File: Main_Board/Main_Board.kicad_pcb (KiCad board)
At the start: 2 copper layers, 3 parts, among them U1 TCR2EF33_LMCT

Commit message: Main board
The schematic is done, tho I have some concerns...
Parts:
- removed C1, C2: C, Capacitor_SMD:C_1206_3216Metric_Pad1.33x1.80mm_HandSolder
- added C3: 10uF, Capacitor_SMD:C_0805_2012Metric_Pad1.18x1.45mm_HandSolder, F.Cu at (173.5, 136.5)
- added C4: 0.1uF, Capacitor_SMD:C_0805_2012Metric_Pad1.18x1.45mm_HandSolder, F.Cu at (163.0, 136.5)
- added C5: 100uF, Capacitor_SMD:C_0805_2012Metric_Pad1.18x1.45mm_HandSolder, F.Cu at (168.5, 136.5)
- added J1: USB_C_Receptacle_USB2.0_16P, Connector_USB:USB_C_Receptacle_HRO_TYPE-C-31-M-17, F.Cu at (156.0, 147.0)
- added J2: Conn_01x04_Pin, Connector_PinHeader_2.54mm:PinHeader_1x01_P2.54mm_Vertical, F.Cu at (148.2, 123.5)
- added J3: Conn_01x05_Pin, Connector_PinHeader_2.54mm:PinHeader_1x01_P2.54mm_Vertical, F.Cu at (172.0, 149.5)
- added J4: Conn_01x03_Pin, Connector_PinHeader_2.54mm:PinHeader_1x01_P2.54mm_Vertical, F.Cu at (141.5, 150.0)
- added L1: L, Inductor_SMD:L_0805_2012Metric, F.Cu at (160.6, 140.0)
- added R1: 10k, Resistor_SMD:R_0805_2012Metric_Pad1.20x1.40mm_HandSolder, F.Cu at (143.5, 122.7)
- added R2: 10K, Resistor_SMD:R_0805_2012Metric_Pad1.20x1.40mm_HandSolder, F.Cu at (143.5, 125.7)
- added R3: 5.1K, Resistor_SMD:R_0805_2012Metric_Pad1.20x1.40mm_HandSolder, F.Cu at (143.5, 128.6)
- added R4: 5.1K, Resistor_SMD:R_0805_2012Metric_Pad1.20x1.40mm_HandSolder, F.Cu at (143.5, 131.6)
- added R5: 4.7K, Resistor_SMD:R_0805_2012Metric_Pad1.20x1.40mm_HandSolder, F.Cu at (143.5, 134.5)
- added R6: 4.7K, Resistor_SMD:R_0805_2012Metric_Pad1.20x1.40mm_HandSolder, F.Cu at (143.5, 137.5)
- added U2: ESP32-WROOM-32, RF_Module:ESP32-WROOM-32, F.Cu at (167.2, 120.4)
- added U3: TLV9001IDCK, Package_TO_SOT_SMD:SOT-353_SC-70-5, F.Cu at (158.1, 132.3)
- U1: value TCR2EF33_LMCT -> DEV-15583; footprint shared_footprints:SOT-25 SMV_TOS -> Connector_PinHeader_2.54mm:PinHeader_2x14_P2.54mm_Vertical
- moved U1 22.2 mm to (182.5, 115.3)
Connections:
- U1 pad 1: Net-(U1-VIN) -> unconnected-(U1-Pad1)
- U1 pad 5: Net-(U1-VOUT) -> unconnected-(U1-Pad5)
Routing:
- net Net-(J4-Pin_1): track 0.00 -> 51.5 mm
- net Net-(U1-VIN): track 16.2 -> 0.00 mm
- net Net-(U1-VOUT): track 10.4 -> 0.00 mm
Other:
- board outline added: 55 x 63 mm

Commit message: updated main PCB
same thing
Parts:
- J1: footprint Connector_USB:USB_C_Receptacle_HRO_TYPE-C-31-M-17 -> Connector_USB:USB_C_Receptacle_HRO_TYPE-C-31-M-12
- J2: footprint Connector_PinHeader_2.54mm:PinHeader_1x01_P2.54mm_Vertical -> Connector_PinHeader_2.54mm:PinHeader_1x04_P2.54mm_Vertical
- J3: footprint Connector_PinHeader_2.54mm:PinHeader_1x01_P2.54mm_Vertical -> Connector_PinHeader_2.54mm:PinHeader_1x05_P2.54mm_Vertical
- J4: footprint Connector_PinHeader_2.54mm:PinHeader_1x01_P2.54mm_Vertical -> Connector_PinHeader_2.54mm:PinHeader_1x03_P2.54mm_Vertical
- U1: footprint Connector_PinHeader_2.54mm:PinHeader_2x14_P2.54mm_Vertical -> shared_footprints:MODULE_DEV-15583
- U2: value ESP32-WROOM-32 -> XIAO-ESP32-C3-DIP; footprint RF_Module:ESP32-WROOM-32 -> RF_Module:MCU_Seeed_ESP32C3
- U3: footprint Package_TO_SOT_SMD:SOT-353_SC-70-5 -> Package_TO_SOT_THT:TO-92_Inline
- moved J3 83.3 mm to (107.0, 97.5)
- moved J2 58.2 mm to (107.0, 82.5)
- moved J4 48.8 mm to (107.0, 115.5)
- moved U3 48.3 mm to (121.1, 101.2), turned to -90 degrees
- moved C3 44.1 mm to (158.5, 95.0)
- moved U1 41.9 mm to (143.1, 100.9)
- moved R1 39.5 mm to (113.5, 97.0)
- moved R2 37.9 mm to (113.5, 102.5)
- moved C4 37.8 mm to (158.5, 99.0)
- moved R4 37.0 mm to (129.0, 97.5)
- moved R3 36.2 mm to (113.5, 108.5)
- moved R5 35.6 mm to (129.0, 102.0)
- moved R6 34.2 mm to (129.0, 106.5)
- moved J1 33.5 mm to (129.5, 126.5)
- moved C5 30.2 mm to (141.6, 122.9), turned to 90 degrees
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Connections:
- R5 pad 2: Net-(U2-IO22) -> Net-(U2-GPIO7/D5/SCL)
- U1 pad 16: Net-(U2-IO22) -> Net-(U2-GPIO7/D5/SCL)
- U1 pad 17: Net-(U2-IO21) -> Net-(U2-GPIO6/D4/SDA)
- U1 pad 18: Net-(U2-SDO/SD0) -> unconnected-(U1-Pad18)
- U1 pad 19: Net-(U2-SENSOR_VN) -> Net-(U2-GPIO3/A1/D1)
- U1 pad 20: Net-(U2-SENSOR_VP) -> Net-(U2-GPIO2/A0/D0)
- U1 pad 21: Net-(U2-EN) -> Net-(U2-GPIO5/A3/D3)
- U2 pad 1: GND -> Net-(U2-GPIO2/A0/D0)
- U2 pad 13: unconnected-(U2-IO14-Pad13) -> GND
- U2 pad 14: unconnected-(U2-IO12-Pad14) -> +5V
- U2 pad 2: unconnected-(U2-VDD-Pad2) -> Net-(U2-GPIO3/A1/D1)
- U2 pad 3: Net-(U2-EN) -> unconnected-(U2-GPIO4/A2/D2-Pad3)
- U2 pad 4: Net-(U2-SENSOR_VP) -> Net-(U2-GPIO5/A3/D3)
- U2 pad 5: Net-(U2-SENSOR_VN) -> Net-(U2-GPIO6/D4/SDA)
- U2 pad 6: unconnected-(U2-IO34-Pad6) -> Net-(U2-GPIO7/D5/SCL)
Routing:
- net +5V: track 0.00 -> 141.0 mm, vias 0 -> 4
- net Net-(J4-Pin_3): track 0.00 -> 95.1 mm, vias 0 -> 4
- net GND: track 0.00 -> 70.2 mm, vias 0 -> 2
- net Net-(J3-Pin_1): track 0.00 -> 60.0 mm, vias 0 -> 2
- net Net-(J4-Pin_2): track 0.00 -> 52.9 mm, vias 0 -> 2
- net Net-(U2-GPIO7/D5/SCL): track 0.00 -> 47.4 mm, vias 0 -> 4
- net Net-(J3-Pin_2): track 0.00 -> 43.5 mm, vias 0 -> 4
- net Net-(J2-Pin_2): track 0.00 -> 41.7 mm
- net Net-(J3-Pin_3): track 0.00 -> 38.8 mm, vias 0 -> 2
- net Net-(J3-Pin_5): track 0.00 -> 33.3 mm, vias 0 -> 2
- net Net-(J3-Pin_4): track 0.00 -> 32.9 mm, vias 0 -> 2
- net Net-(J1-CC1): track 0.00 -> 28.0 mm, vias 0 -> 2
- net Net-(U2-GPIO5/A3/D3): track 0.00 -> 26.3 mm, vias 0 -> 2
- net Net-(U2-GPIO6/D4/SDA): track 0.00 -> 18.2 mm
- net Net-(U2-GPIO3/A1/D1): track 0.00 -> 15.7 mm
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- added copper zone on B.Cu, net GND
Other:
- board size 55 x 63 mm -> 73 x 51.5 mm

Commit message: jst sh
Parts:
- removed J2: Conn_01x04_Pin, Connector_PinHeader_2.54mm:PinHeader_1x04_P2.54mm_Vertical
- added C1: 10μF, Capacitor_SMD:C_0805_2012Metric_Pad1.18x1.45mm_HandSolder, F.Cu at (93.2, 113.2)
- added J5: Conn_01x03_Pin, Connector_JST:JST_SH_SM02B-SRSS-TB_1x02-1MP_P1.00mm_Horizontal, F.Cu at (94.2, 107.9)
- added R6: 4.7K, Resistor_SMD:R_0805_2012Metric_Pad1.20x1.40mm_HandSolder, F.Cu at (100.0, 105.6)
- added R7: 1000KΩ, Resistor_SMD:R_0805_2012Metric_Pad1.20x1.40mm_HandSolder, F.Cu at (100.0, 108.5)
- added R8: 47KΩ, Resistor_SMD:R_0805_2012Metric_Pad1.20x1.40mm_HandSolder, F.Cu at (100.0, 111.5)
- added U4: NE555D, Package_SO:SOIC-8_3.9x4.9mm_P1.27mm, F.Cu at (95.0, 100.9)
- J3: footprint Connector_PinHeader_2.54mm:PinHeader_1x05_P2.54mm_Vertical -> Connector_JST:JST_SH_SM05B-SRSS-TB_1x05-1MP_P1.00mm_Horizontal
- J4: footprint Connector_PinHeader_2.54mm:PinHeader_1x03_P2.54mm_Vertical -> Connector_JST:JST_SH_SM03B-SRSS-TB_1x03-1MP_P1.00mm_Horizontal
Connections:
- net Net-(U2-GPIO3/A1/D1) renamed GPI03
- net Net-(U2-GPIO5/A3/D3) renamed GPIO5
- net Net-(U2-GPIO6/D4/SDA) renamed SDA
- J1 pad A1: +5V -> GND
- J1 pad A12: +5V -> GND
- J1 pad A4: Net-(J1-VBUS-PadA4) -> +5V
- J1 pad A9: Net-(J1-VBUS-PadA4) -> +5V
- J1 pad B1: +5V -> GND
- J1 pad B12: +5V -> GND
- J1 pad B4: Net-(J1-VBUS-PadA4) -> +5V
- J1 pad B9: Net-(J1-VBUS-PadA4) -> +5V
- J1 pad S1: unconnected-(J1-SHIELD-PadS1)_3 -> GND
- R5 pad 2: Net-(U2-GPIO7/D5/SCL) -> SCl
- U1 pad 16: Net-(U2-GPIO7/D5/SCL) -> SCL
- U1 pad 20: Net-(U2-GPIO2/A0/D0) -> GPI02
- U1 pad 3.3V_2: unconnected-(U1-Pad3.3V_2) -> +3.3V
- U2 pad 1: Net-(U2-GPIO2/A0/D0) -> GPIO2
- U2 pad 6: Net-(U2-GPIO7/D5/SCL) -> SCl
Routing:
- net (no net): track 0.00 -> 63.1 mm, vias 0 -> 4
- net Net-(U2-GPIO7/D5/SCL): track 47.4 -> 0.00 mm, vias 4 -> 0
- net Net-(U2-GPIO2/A0/D0): track 15.7 -> 0.00 mm
- net Net-(J1-VBUS-PadA4): vias 2 -> 0
- net +5V: vias 4 -> 6

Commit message: Updated Main board
not done yet but putting here
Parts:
- added REF**: MountingHole_3.2mm_M3, MountingHole:MountingHole_3.2mm_M3, F.Cu at (83.3, 79.4)
- added REF**: MountingHole_3.2mm_M3, MountingHole:MountingHole_3.2mm_M3, F.Cu at (82.5, 119.5)
- added REF**: MountingHole_3.2mm_M3, MountingHole:MountingHole_3.2mm_M3, F.Cu at (189.0, 80.0)
- added REF**: MountingHole_3.2mm_M3, MountingHole:MountingHole_3.2mm_M3, F.Cu at (190.2, 118.5)
- moved C5 21.9 mm to (162.5, 116.4)
- moved C1 20.3 mm to (113.3, 115.7)
- moved U2 20.3 mm to (174.7, 101.8)
- moved L1 20.1 mm to (156.6, 116.2)
- moved U4 19.2 mm to (104.7, 117.5)
- moved R6 13.3 mm to (113.1, 103.4)
- moved R7 13.3 mm to (113.1, 106.3)
- moved R8 13.3 mm to (113.1, 109.3)
- moved J3 12.6 mm to (98.9, 87.8), turned to -90 degrees
- moved J1 11.9 mm to (124.5, 115.7)
- moved J5 10.3 mm to (99.1, 98.8), turned to -90 degrees
- moved J4 9.67 mm to (99.2, 109.8), turned to -90 degrees
- moved R1 9.29 mm to (112.9, 87.7)
- moved R2 9.29 mm to (112.9, 93.2)
- moved R3 9.29 mm to (112.9, 99.2)
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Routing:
- net +5V: track 141.0 -> 17.4 mm, vias 6 -> 0
- net (no net): track 63.1 -> 0.00 mm, vias 4 -> 0
- net Net-(J4-Pin_1): track 53.6 -> 0.00 mm, vias 2 -> 0
- net GND: track 70.2 -> 16.7 mm
- net Net-(J4-Pin_2): track 52.9 -> 2.75 mm, vias 2 -> 1
- net Net-(J3-Pin_1): track 60.0 -> 17.9 mm, vias 2 -> 1
- net Net-(U3-+): track 41.7 -> 1.00 mm
- net Net-(J3-Pin_2): track 43.5 -> 3.54 mm, vias 4 -> 0
- net Net-(J3-Pin_3): track 38.8 -> 2.12 mm, vias 2 -> 1
- net Net-(J3-Pin_5): track 33.3 -> 0.00 mm, vias 2 -> 0
- net Net-(J3-Pin_4): track 32.9 -> 0.00 mm, vias 2 -> 0
- net Net-(J4-Pin_3): track 95.1 -> 62.8 mm, vias 4 -> 3
- net Net-(J1-CC1): track 28.0 -> 0.00 mm, vias 2 -> 0
- net GPIO5: track 26.3 -> 0.00 mm, vias 2 -> 0
- net SDA: track 18.2 -> 0.00 mm
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- removed copper zone on B.Cu, net GND
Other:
- board outline removed

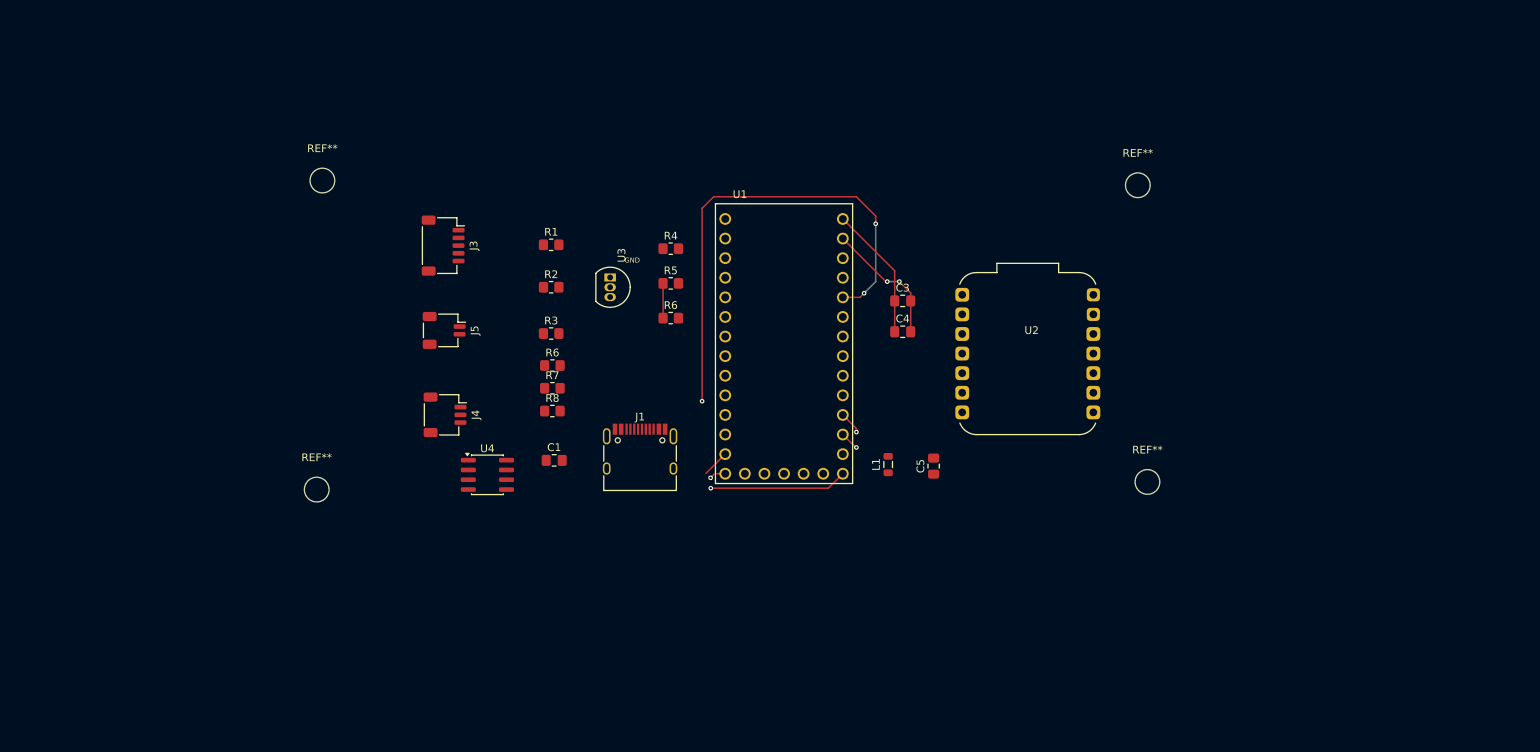
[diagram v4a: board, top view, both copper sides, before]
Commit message: replaced opamp with LDO, completed layout
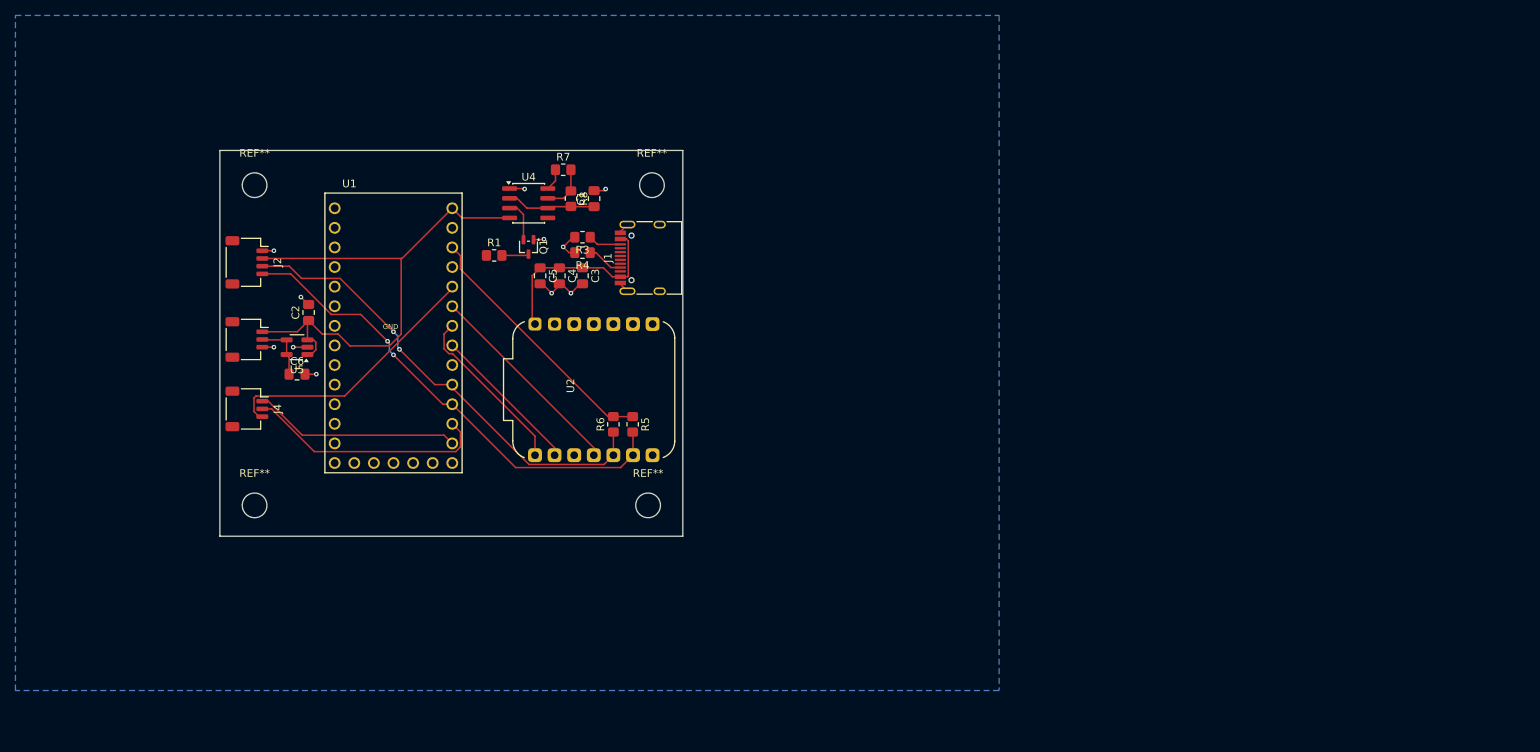
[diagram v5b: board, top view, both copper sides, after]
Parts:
- removed J3: Conn_01x05_Pin, Connector_JST:JST_SH_SM05B-SRSS-TB_1x05-1MP_P1.00mm_Horizontal
- removed L1: L, Inductor_SMD:L_0805_2012Metric
- removed R2: 10K, Resistor_SMD:R_0805_2012Metric_Pad1.20x1.40mm_HandSolder
- removed the R6 at (128.4, 97.2)
- removed U3: TLV9001IDCK, Package_TO_SOT_THT:TO-92_Inline
- added C2: 0.1uF, Capacitor_SMD:C_0805_2012Metric_Pad1.18x1.45mm_HandSolder, F.Cu at (81.5, 96.5)
- added C6: 0.1uF, Capacitor_SMD:C_0805_2012Metric_Pad1.18x1.45mm_HandSolder, F.Cu at (80.0, 104.5)
- added J2: Conn_01x04_Pin, Connector_JST:JST_SH_SM04B-SRSS-TB_1x04-1MP_P1.00mm_Horizontal, F.Cu at (73.5, 90.0)
- added Q1: NMOS, Package_TO_SOT_SMD:SOT-323_SC-70, F.Cu at (110.0, 88.0)
- added U5: TPS72101DBVR, Package_TO_SOT_SMD:SOT-23-5_HandSoldering, F.Cu at (80.0, 101.0)
- J5: footprint Connector_JST:JST_SH_SM02B-SRSS-TB_1x02-1MP_P1.00mm_Horizontal -> Connector_JST:JST_SH_SM03B-SRSS-TB_1x03-1MP_P1.00mm_Horizontal
- R1: value 10k -> 30
- moved REF** 64.8 mm to (125.5, 121.5)
- moved REF** 63.0 mm to (126.0, 80.0)
- moved C5 56.7 mm to (111.5, 91.7), turned to -90 degrees
- moved U2 56.4 mm to (118.5, 106.5), turned to 90 degrees
- moved U1 50.6 mm to (92.5, 99.5)
- moved C4 45.1 mm to (114.0, 91.7), turned to -90 degrees
- moved C3 41.6 mm to (117.0, 91.7), turned to -90 degrees
- moved U4 35.6 mm to (110.0, 82.3)
- moved C1 34.3 mm to (118.5, 81.7), turned to 90 degrees
- moved R7 28.4 mm to (114.5, 78.0)
- moved R8 27.6 mm to (115.5, 81.7), turned to -90 degrees
- moved J1 26.3 mm to (126.0, 89.4), turned to 90 degrees
- moved J4 25.7 mm to (73.5, 109.0)
- moved J5 25.6 mm to (73.5, 100.0)
- moved R5 18.9 mm to (123.5, 111.0), turned to -90 degrees
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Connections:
- R5 pad 2: SCl -> SCL
- R7 pad 1: 5V -> +5V
- U1 pad 10: Net-(J3-Pin_5) -> unconnected-(U1-Pad10)
- U1 pad 11: Net-(J3-Pin_2) -> unconnected-(U1-Pad11)
- U1 pad 12: Net-(J3-Pin_3) -> unconnected-(U1-Pad12)
- U1 pad 13: Net-(J3-Pin_1) -> unconnected-(U1-Pad13)
- U1 pad 20: GPI02 -> GPIO2
- U1 pad 9: Net-(J3-Pin_4) -> unconnected-(U1-Pad9)
- U2 pad 6: SCl -> SCL
- U4 pad 3: output -> Net-(Q1-G)
- U4 pad 4: 5V -> +5V
- U4 pad 8: 5V -> +5V
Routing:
- net +5V: track 17.4 -> 100.1 mm
- net SDA: track 0.00 -> 60.8 mm, vias 0 -> 2
- net SCL: track 2.95 -> 62.7 mm, vias 1 -> 2
- net +3.3V: track 4.50 -> 33.5 mm
- net Net-(J4-Pin_2): track 2.75 -> 31.7 mm, vias 1 -> 0
- net Net-(J4-Pin_3): track 62.8 -> 34.9 mm, vias 3 -> 0
- net GPIO5: track 0.00 -> 26.9 mm
- net Net-(J4-Pin_1): track 0.00 -> 26.9 mm
- net GPIO2: track 0.00 -> 22.4 mm
- net GPI03: track 0.00 -> 19.7 mm
- net Net-(J3-Pin_1): track 17.9 -> 0.00 mm, vias 1 -> 0
- net Net-(U4-THR): track 0.00 -> 11.6 mm
- net GND: track 16.7 -> 27.0 mm, vias 2 -> 11
- net 2.5V: track 0.00 -> 7.75 mm
- net Net-(U4-DIS): track 0.00 -> 6.14 mm
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- added copper zone on B.Cu, net GND
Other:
- board outline added: 60 x 50 mm
